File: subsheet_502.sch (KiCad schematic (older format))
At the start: 26 parts, among them U500 74F374_OCTAL_D-TYPE_EDGE-TRIG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, U501 74F374_OCTAL_D-TYPE_EDGE-TRIG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, U502 DAC0802LCN_PHY, U503 DAC0802LCN_PHY

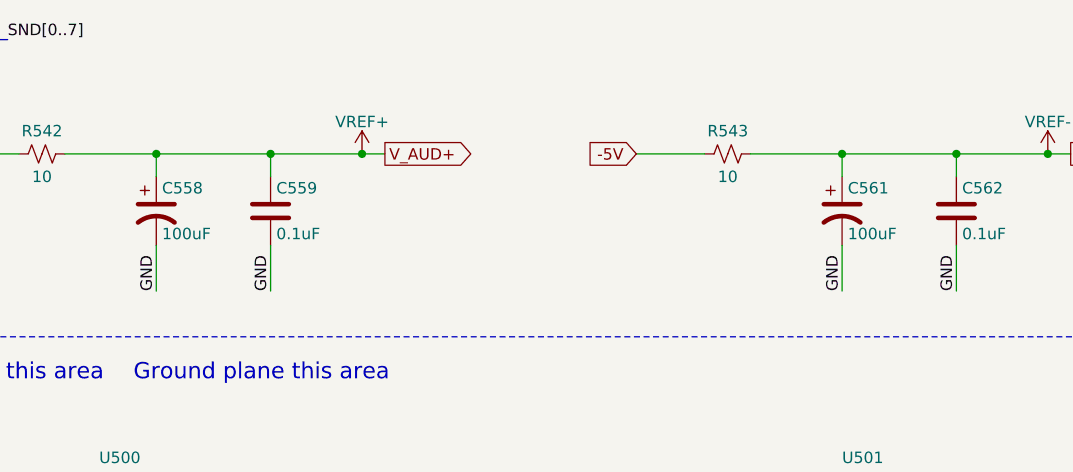
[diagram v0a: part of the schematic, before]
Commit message: Resolves #12 : Use the reference 'CP?' for polarized capacitors
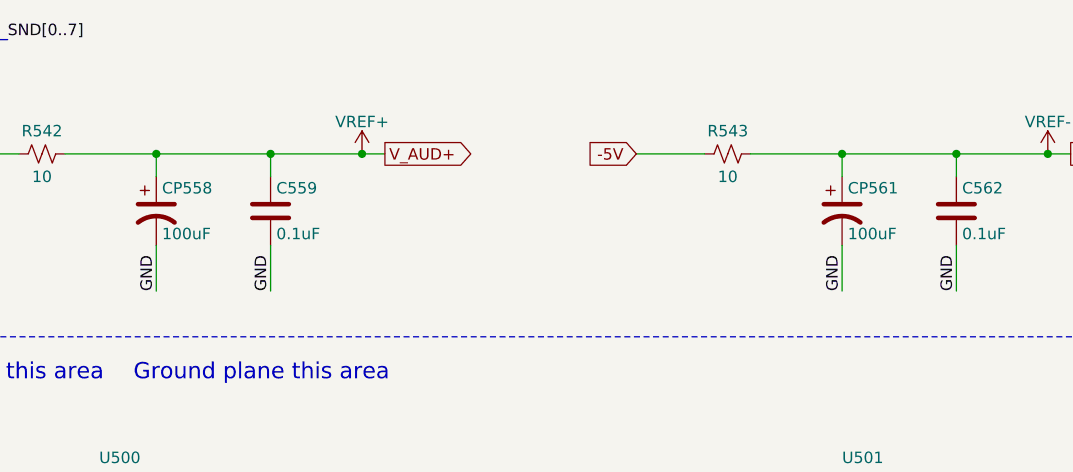
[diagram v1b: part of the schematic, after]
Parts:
- renumbered C558 to CP558, C561 to CP561
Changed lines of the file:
@@
 AR Path="/6089D0C2/60CB5FED" Ref="C?"  Part="1"
 AR Path="/60B8B7AD/60CB5FED" Ref="C?"  Part="1"
-AR Path="/60C95DE8/60CB5FED" Ref="C558"  Part="1"
-F 0 "C558" H 2425 1850 50  0000 L CNN
+AR Path="/60C95DE8/60CB5FED" Ref="CP558"  Part="1"
+F 0 "CP558" H 2425 1850 50  0000 L CNN
 F 1 "100uF" H 2425 1650 50  0000 L CNN
 F 2 "commons_passives_THT:Passive_THT_capacitor_polarized_W6.35mm_L20.32mm" H 2400 1750 50  0001 C CNN
@@
 AR Path="/6089D0C2/60CB9C69" Ref="C?"  Part="1"
 AR Path="/60B8B7AD/60CB9C69" Ref="C?"  Part="1"
-AR Path="/60C95DE8/60CB9C69" Ref="C561"  Part="1"
-F 0 "C561" H 5425 1850 50  0000 L CNN
+AR Path="/60C95DE8/60CB9C69" Ref="CP561"  Part="1"
+F 0 "CP561" H 5425 1850 50  0000 L CNN
 F 1 "100uF" H 5425 1650 50  0000 L CNN
 F 2 "commons_passives_THT:Passive_THT_capacitor_polarized_W6.35mm_L20.32mm" H 5400 1750 50  0001 C CNN

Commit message: Resolves #13 : assign 1206 hand-solder footprints to resistors
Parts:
- R500, R505, R506, R508, R509, R514, R515, R517, R542, R543: footprint commons_passives_THT:Passive_THT_resistor_W2.54mm_L12.70mm -> Resistor_SMD:R_1206_3216Metric_Pad1.30x1.75mm_HandSolder
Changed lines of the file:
@@
 F 0 "R542" V 1800 1500 50  0000 C CNN
 F 1 "10" V 2000 1500 50  0000 C CNN
-F 2 "commons_passives_THT:Passive_THT_resistor_W2.54mm_L12.70mm" H 1900 1500 50  0001 C CNN
+F 2 "Resistor_SMD:R_1206_3216Metric_Pad1.30x1.75mm_HandSolder" H 1900 1500 50  0001 C CNN
 F 3 "~" H 1900 1500 50  0001 C CNN
 	1    1900 1500
@@
 F 0 "R543" V 4800 1500 50  0000 C CNN
 F 1 "10" V 5000 1500 50  0000 C CNN
-F 2 "commons_passives_THT:Passive_THT_resistor_W2.54mm_L12.70mm" H 4900 1500 50  0001 C CNN
+F 2 "Resistor_SMD:R_1206_3216Metric_Pad1.30x1.75mm_HandSolder" H 4900 1500 50  0001 C CNN
 F 3 "~" H 4900 1500 50  0001 C CNN
 	1    4900 1500
@@
 F 0 "R505" H 2100 5450 50  0000 L CNN
 F 1 "10K" H 2150 5350 50  0000 L CNN
-F 2 "commons_passives_THT:Passive_THT_resistor_W2.54mm_L12.70mm" H 2350 5400 50  0001 C CNN
+F 2 "Resistor_SMD:R_1206_3216Metric_Pad1.30x1.75mm_HandSolder" H 2350 5400 50  0001 C CNN
 F 3 "~" H 2350 5400 50  0001 C CNN
 	1    2350 5400
@@
 F 0 "R506" H 1300 5900 50  0000 L CNN
 F 1 "10K 1%" H 1300 5800 50  0000 L CNN
-F 2 "commons_passives_THT:Passive_THT_resistor_W2.54mm_L12.70mm" H 1250 5900 50  0001 C CNN
+F 2 "Resistor_SMD:R_1206_3216Metric_Pad1.30x1.75mm_HandSolder" H 1250 5900 50  0001 C CNN
 F 3 "~" H 1250 5900 50  0001 C CNN
 	1    1250 5900
@@
 F 0 "R500" H 2200 8550 50  0000 L CNN
 F 1 "8K2 1%" H 2100 8650 50  0000 L CNN
-F 2 "commons_passives_THT:Passive_THT_resistor_W2.54mm_L12.70mm" H 2450 8600 50  0001 C CNN
+F 2 "Resistor_SMD:R_1206_3216Metric_Pad1.30x1.75mm_HandSolder" H 2450 8600 50  0001 C CNN
 F 3 "~" H 2450 8600 50  0001 C CNN
 	1    2450 8600
@@
 F 0 "R508" H 2350 8550 50  0000 L CNN
 F 1 "8K2 1%" H 2350 8650 50  0000 L CNN
-F 2 "commons_passives_THT:Passive_THT_resistor_W2.54mm_L12.70mm" H 2250 8600 50  0001 C CNN
+F 2 "Resistor_SMD:R_1206_3216Metric_Pad1.30x1.75mm_HandSolder" H 2250 8600 50  0001 C CNN
 F 3 "~" H 2250 8600 50  0001 C CNN
 	1    2250 8600
@@
 F 0 "R514" H 5600 5450 50  0000 L CNN
 F 1 "10K" H 5650 5350 50  0000 L CNN
-F 2 "commons_passives_THT:Passive_THT_resistor_W2.54mm_L12.70mm" H 5850 5400 50  0001 C CNN
+F 2 "Resistor_SMD:R_1206_3216Metric_Pad1.30x1.75mm_HandSolder" H 5850 5400 50  0001 C CNN
 F 3 "~" H 5850 5400 50  0001 C CNN
 	1    5850 5400
@@
 F 0 "R515" H 4800 5900 50  0000 L CNN
 F 1 "10K 1%" H 4800 5800 50  0000 L CNN
-F 2 "commons_passives_THT:Passive_THT_resistor_W2.54mm_L12.70mm" H 4750 5900 50  0001 C CNN
+F 2 "Resistor_SMD:R_1206_3216Metric_Pad1.30x1.75mm_HandSolder" H 4750 5900 50  0001 C CNN
 F 3 "~" H 4750 5900 50  0001 C CNN
 	1    4750 5900
@@
 F 0 "R509" H 5700 8550 50  0000 L CNN
 F 1 "8K2 1%" H 5600 8650 50  0000 L CNN
-F 2 "commons_passives_THT:Passive_THT_resistor_W2.54mm_L12.70mm" H 5950 8600 50  0001 C CNN
+F 2 "Resistor_SMD:R_1206_3216Metric_Pad1.30x1.75mm_HandSolder" H 5950 8600 50  0001 C CNN
 F 3 "~" H 5950 8600 50  0001 C CNN
 	1    5950 8600
@@
 F 0 "R517" H 5800 8550 50  0000 L CNN
 F 1 "8K2 1%" H 5800 8650 50  0000 L CNN
-F 2 "commons_passives_THT:Passive_THT_resistor_W2.54mm_L12.70mm" H 5750 8600 50  0001 C CNN
+F 2 "Resistor_SMD:R_1206_3216Metric_Pad1.30x1.75mm_HandSolder" H 5750 8600 50  0001 C CNN
 F 3 "~" H 5750 8600 50  0001 C CNN
 	1    5750 8600

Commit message: Resolves #8 : Assign 1206 hand-solder footprints to non polarized capacitors
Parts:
- C503, C515: footprint commons_passives_THT:Passive_THT_capacitor_W2.54mm_L10.16mm -> Capacitor_SMD:C_1206_3216Metric_Pad1.33x1.80mm_HandSolder
- C504, C507, C516, C519, C556, C557, C559, C562: footprint commons_passives_THT:Passive_THT_capacitor_mlcc_W2.54mm_L7.62mm -> Capacitor_SMD:C_1206_3216Metric_Pad1.33x1.80mm_HandSolder
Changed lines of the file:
@@
 F 0 "C559" H 2925 1850 50  0000 L CNN
 F 1 "0.1uF" H 2925 1650 50  0000 L CNN
-F 2 "commons_passives_THT:Passive_THT_capacitor_mlcc_W2.54mm_L7.62mm" H 2938 1600 50  0001 C CNN
+F 2 "Capacitor_SMD:C_1206_3216Metric_Pad1.33x1.80mm_HandSolder" H 2938 1600 50  0001 C CNN
 F 3 "~" H 2900 1750 50  0001 C CNN
 	1    2900 1750
@@
 F 0 "C562" H 5925 1850 50  0000 L CNN
 F 1 "0.1uF" H 5925 1650 50  0000 L CNN
-F 2 "commons_passives_THT:Passive_THT_capacitor_mlcc_W2.54mm_L7.62mm" H 5938 1600 50  0001 C CNN
+F 2 "Capacitor_SMD:C_1206_3216Metric_Pad1.33x1.80mm_HandSolder" H 5938 1600 50  0001 C CNN
 F 3 "~" H 5900 1750 50  0001 C CNN
 	1    5900 1750
@@
 F 0 "C503" H 1675 6000 50  0000 L CNN
 F 1 "0.01uF" H 1675 5800 50  0000 L CNN
-F 2 "commons_passives_THT:Passive_THT_capacitor_W2.54mm_L10.16mm" H 1688 5750 50  0001 C CNN
+F 2 "Capacitor_SMD:C_1206_3216Metric_Pad1.33x1.80mm_HandSolder" H 1688 5750 50  0001 C CNN
 F 3 "~" H 1650 5900 50  0001 C CNN
 	1    1650 5900
@@
 F 0 "C507" H 3475 6600 50  0000 L CNN
 F 1 "0.1uF" H 3475 6400 50  0000 L CNN
-F 2 "commons_passives_THT:Passive_THT_capacitor_mlcc_W2.54mm_L7.62mm" H 3488 6350 50  0001 C CNN
+F 2 "Capacitor_SMD:C_1206_3216Metric_Pad1.33x1.80mm_HandSolder" H 3488 6350 50  0001 C CNN
 F 3 "~" H 3450 6500 50  0001 C CNN
 	1    3450 6500
@@
 F 0 "C504" H 3475 7200 50  0000 L CNN
 F 1 "0.1uF" H 3475 7000 50  0000 L CNN
-F 2 "commons_passives_THT:Passive_THT_capacitor_mlcc_W2.54mm_L7.62mm" H 3488 6950 50  0001 C CNN
+F 2 "Capacitor_SMD:C_1206_3216Metric_Pad1.33x1.80mm_HandSolder" H 3488 6950 50  0001 C CNN
 F 3 "~" H 3450 7100 50  0001 C CNN
 	1    3450 7100
@@
 F 0 "C556" H 1025 4100 50  0000 L CNN
 F 1 "0.1uF" H 1025 3900 50  0000 L CNN
-F 2 "commons_passives_THT:Passive_THT_capacitor_mlcc_W2.54mm_L7.62mm" H 1038 3850 50  0001 C CNN
+F 2 "Capacitor_SMD:C_1206_3216Metric_Pad1.33x1.80mm_HandSolder" H 1038 3850 50  0001 C CNN
 F 3 "~" H 1000 4000 50  0001 C CNN
 	1    1000 4000
@@
 F 0 "C515" H 5175 6000 50  0000 L CNN
 F 1 "0.01uF" H 5175 5800 50  0000 L CNN
-F 2 "commons_passives_THT:Passive_THT_capacitor_W2.54mm_L10.16mm" H 5188 5750 50  0001 C CNN
+F 2 "Capacitor_SMD:C_1206_3216Metric_Pad1.33x1.80mm_HandSolder" H 5188 5750 50  0001 C CNN
 F 3 "~" H 5150 5900 50  0001 C CNN
 	1    5150 5900
@@
 F 0 "C519" H 6975 6600 50  0000 L CNN
 F 1 "0.1uF" H 6975 6400 50  0000 L CNN
-F 2 "commons_passives_THT:Passive_THT_capacitor_mlcc_W2.54mm_L7.62mm" H 6988 6350 50  0001 C CNN
+F 2 "Capacitor_SMD:C_1206_3216Metric_Pad1.33x1.80mm_HandSolder" H 6988 6350 50  0001 C CNN
 F 3 "~" H 6950 6500 50  0001 C CNN
 	1    6950 6500
@@
 F 0 "C516" H 6975 7200 50  0000 L CNN
 F 1 "0.1uF" H 6975 7000 50  0000 L CNN
-F 2 "commons_passives_THT:Passive_THT_capacitor_mlcc_W2.54mm_L7.62mm" H 6988 6950 50  0001 C CNN
+F 2 "Capacitor_SMD:C_1206_3216Metric_Pad1.33x1.80mm_HandSolder" H 6988 6950 50  0001 C CNN
 F 3 "~" H 6950 7100 50  0001 C CNN
 	1    6950 7100
@@
 F 0 "C557" H 7275 4100 50  0000 L CNN
 F 1 "0.1uF" H 7275 3900 50  0000 L CNN
-F 2 "commons_passives_THT:Passive_THT_capacitor_mlcc_W2.54mm_L7.62mm" H 7288 3850 50  0001 C CNN
+F 2 "Capacitor_SMD:C_1206_3216Metric_Pad1.33x1.80mm_HandSolder" H 7288 3850 50  0001 C CNN
 F 3 "~" H 7250 4000 50  0001 C CNN
 	1    7250 4000

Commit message: Resolves #9 : Assign radial THT footprints to polarized capacitors
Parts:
- CP558, CP561: footprint commons_passives_THT:Passive_THT_capacitor_polarized_W6.35mm_L20.32mm -> Capacitor_THT:C_Radial_D8.0mm_H11.5mm_P3.50mm
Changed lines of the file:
@@
 F 0 "CP558" H 2425 1850 50  0000 L CNN
 F 1 "100uF" H 2425 1650 50  0000 L CNN
-F 2 "commons_passives_THT:Passive_THT_capacitor_polarized_W6.35mm_L20.32mm" H 2400 1750 50  0001 C CNN
+F 2 "Capacitor_THT:C_Radial_D8.0mm_H11.5mm_P3.50mm" H 2400 1750 50  0001 C CNN
 F 3 "~" H 2400 1750 50  0001 C CNN
 	1    2400 1750
@@
 F 0 "CP561" H 5425 1850 50  0000 L CNN
 F 1 "100uF" H 5425 1650 50  0000 L CNN
-F 2 "commons_passives_THT:Passive_THT_capacitor_polarized_W6.35mm_L20.32mm" H 5400 1750 50  0001 C CNN
+F 2 "Capacitor_THT:C_Radial_D8.0mm_H11.5mm_P3.50mm" H 5400 1750 50  0001 C CNN
 F 3 "~" H 5400 1750 50  0001 C CNN
 	1    5400 1750
